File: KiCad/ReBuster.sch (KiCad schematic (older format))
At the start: 11 parts, among them U3 SN74CBTD16210, U4 SN74LVC16T245DGVR, U5 SN74CBTD16210, U6 SN74CBTD16210, U7 74LVC2T45DC, U8 PLCC_84_plug, U9 PLCC_84_plug

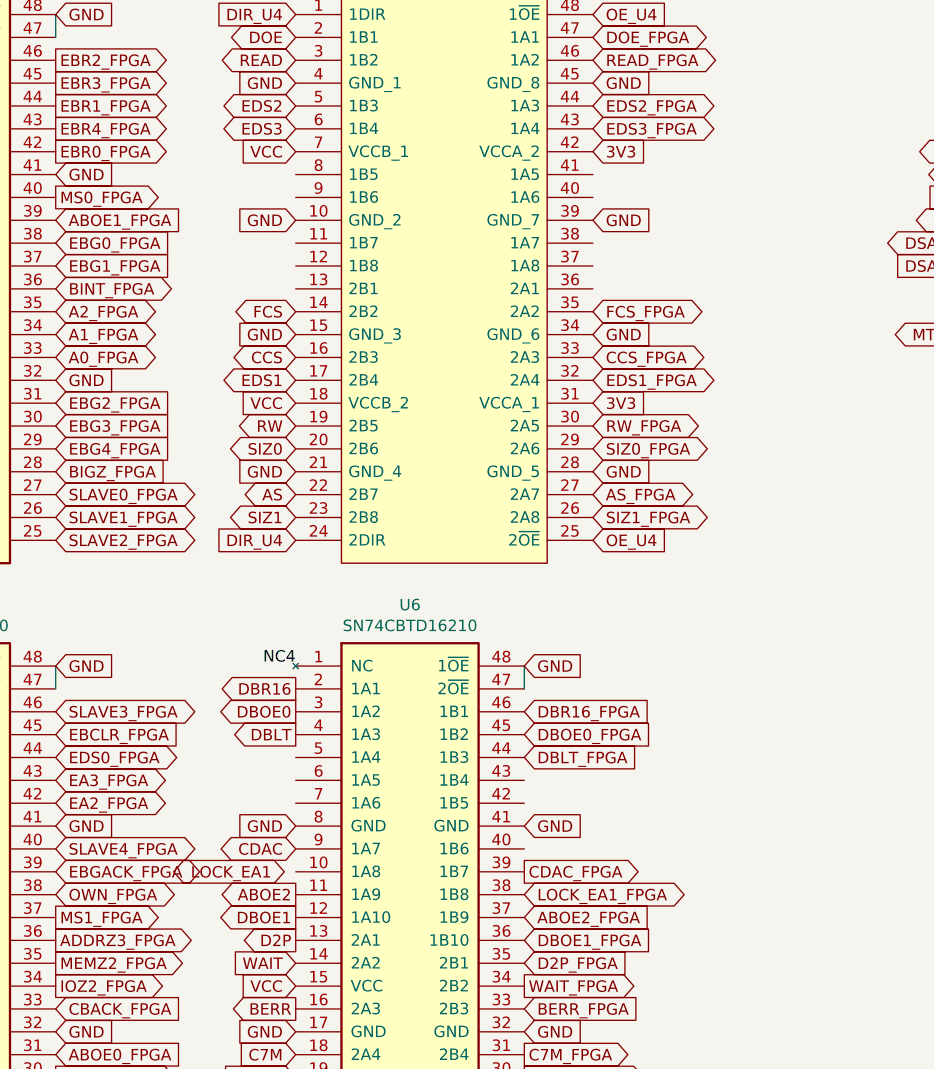
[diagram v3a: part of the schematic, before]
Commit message: Route EA1_LOCK to U4 (SN74LVC16T245DGVR) change K10 -> N4 in FPGA
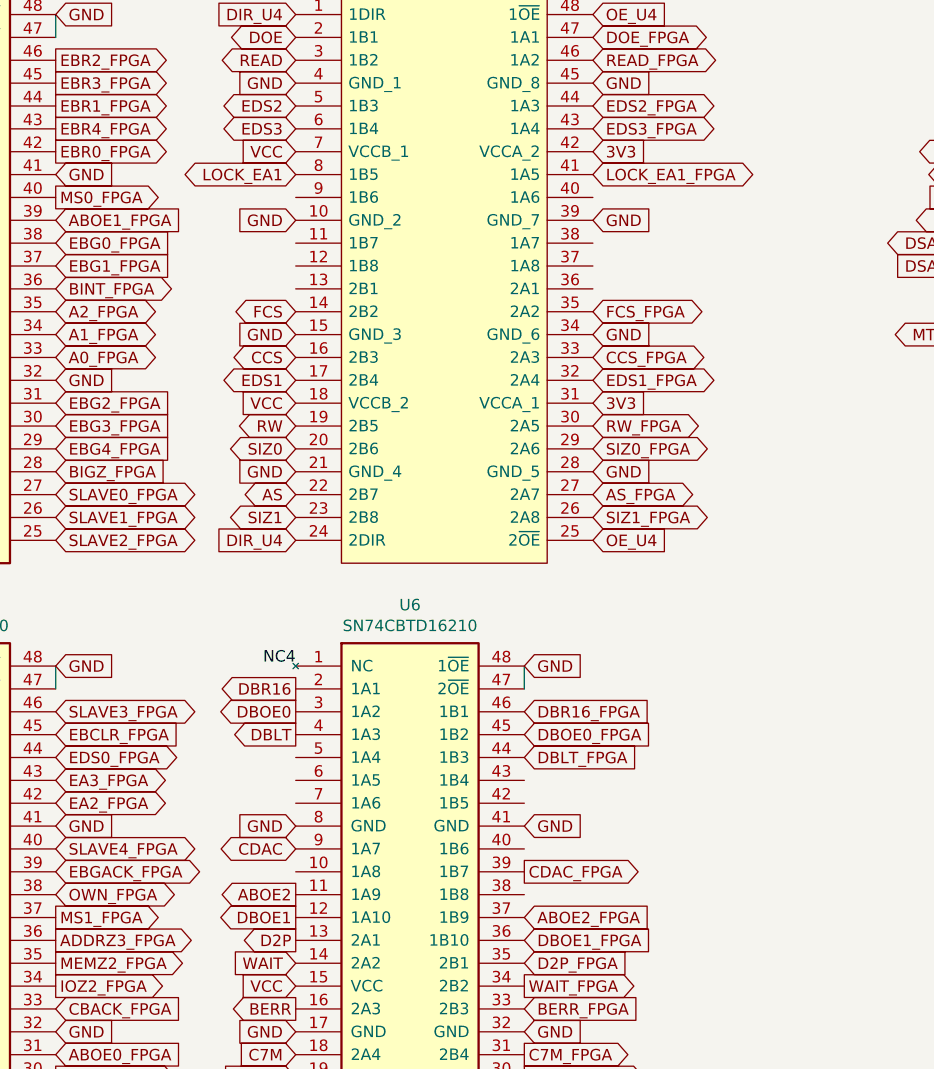
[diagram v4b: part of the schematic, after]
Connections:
- net LOCK_EA1: now also U4.8 (1B5)
- net LOCK_EA1_FPGA: now also U4.41 (1A5); no longer U6.38 (1B8)
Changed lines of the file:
@@
 Text GLabel 10200 4700 2    50   Output ~ 0
 CDAC_FPGA
-Text GLabel 10200 4800 2    50   BiDi ~ 0
+Text GLabel 10500 1650 2    50   BiDi ~ 0
 LOCK_EA1_FPGA
 Text GLabel 10200 4900 2    50   Input ~ 0
@@
 Text GLabel 9200 1450 0    50   BiDi ~ 0
 EDS3
-Text GLabel 9150 4700 0    50   BiDi ~ 0
+Text GLabel 9200 1650 0    50   BiDi ~ 0
 LOCK_EA1
 Text GLabel 9200 4800 0    50   Output ~ 0

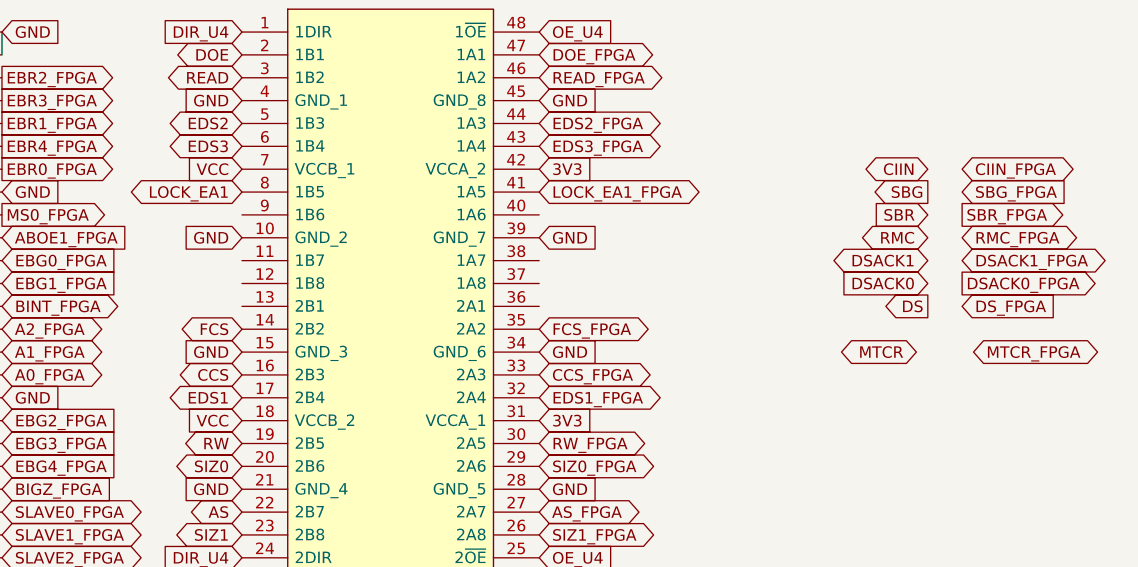
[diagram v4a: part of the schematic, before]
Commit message: Route MTCR to U4 (SN74LVC16T245DGVR) change F12 -> N5 in FPGA
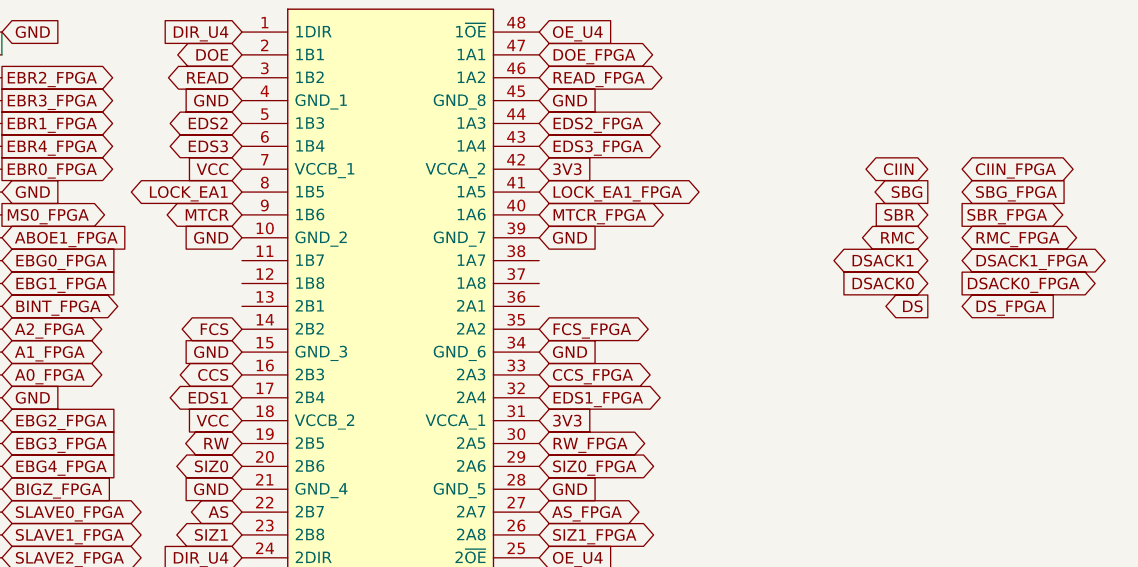
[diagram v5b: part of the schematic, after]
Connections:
- net MTCR: now also U4.9 (1B6)
- net MTCR_FPGA: now also U4.40 (1A6)
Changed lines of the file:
@@
 Text GLabel 8150 5700 2    50   Output ~ 0
 MS2_FPGA
-Text GLabel 12400 2350 2    50   BiDi ~ 0
+Text GLabel 10500 1750 2    50   BiDi ~ 0
 MTCR_FPGA
 Text GLabel 8150 5900 2    50   BiDi ~ 0
@@
 Text GLabel 7150 5700 0    50   Input ~ 0
 MS2
-Text GLabel 12150 2350 0    50   BiDi ~ 0
+Text GLabel 9200 1750 0    50   BiDi ~ 0
 MTCR
 Text GLabel 2750 4650 2    50   Output ~ 0

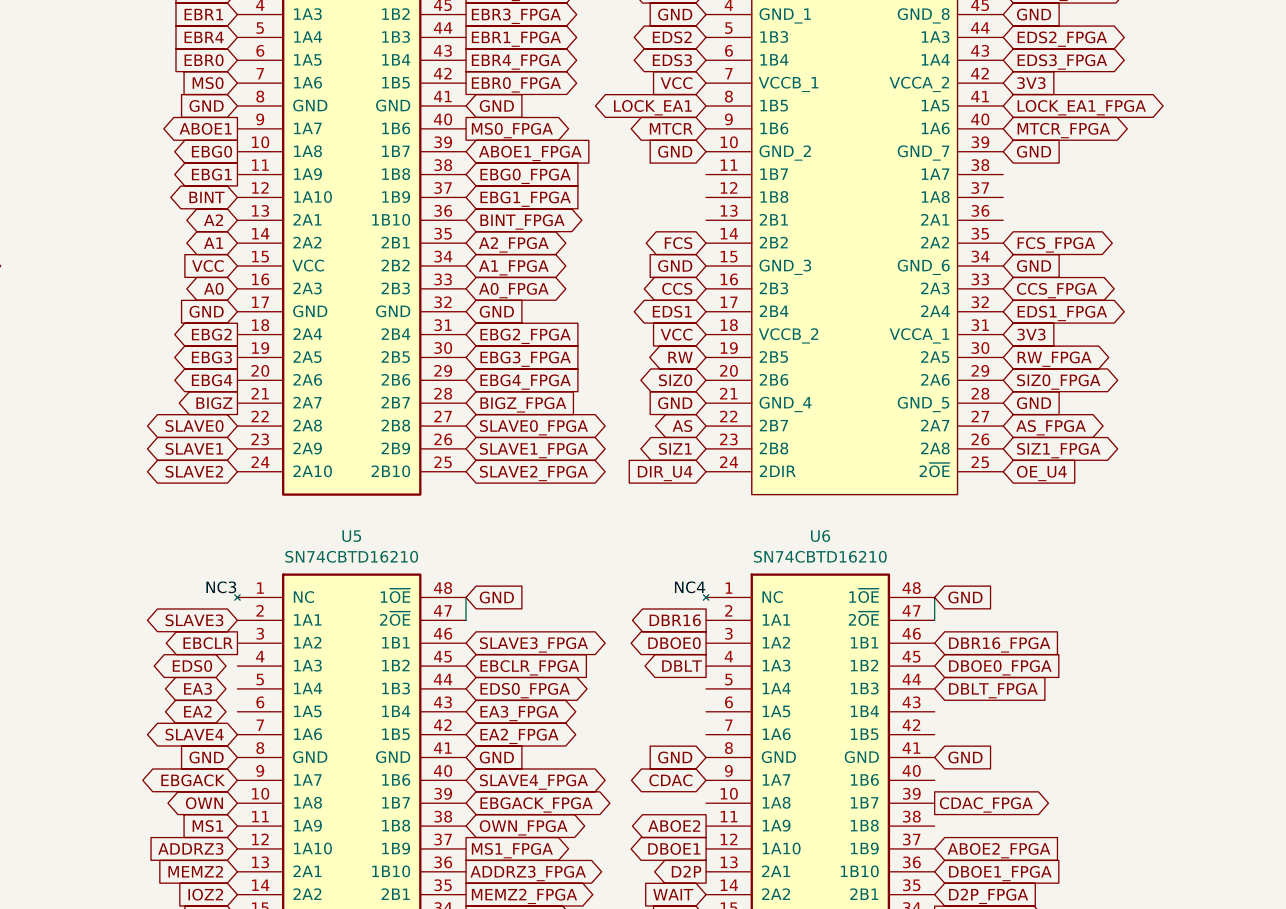
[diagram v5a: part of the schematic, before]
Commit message: Route EA2,EA3 to U4 (SN74LVC16T245DGVR) change D6 -> N6, B5 -> N7 in FPGA
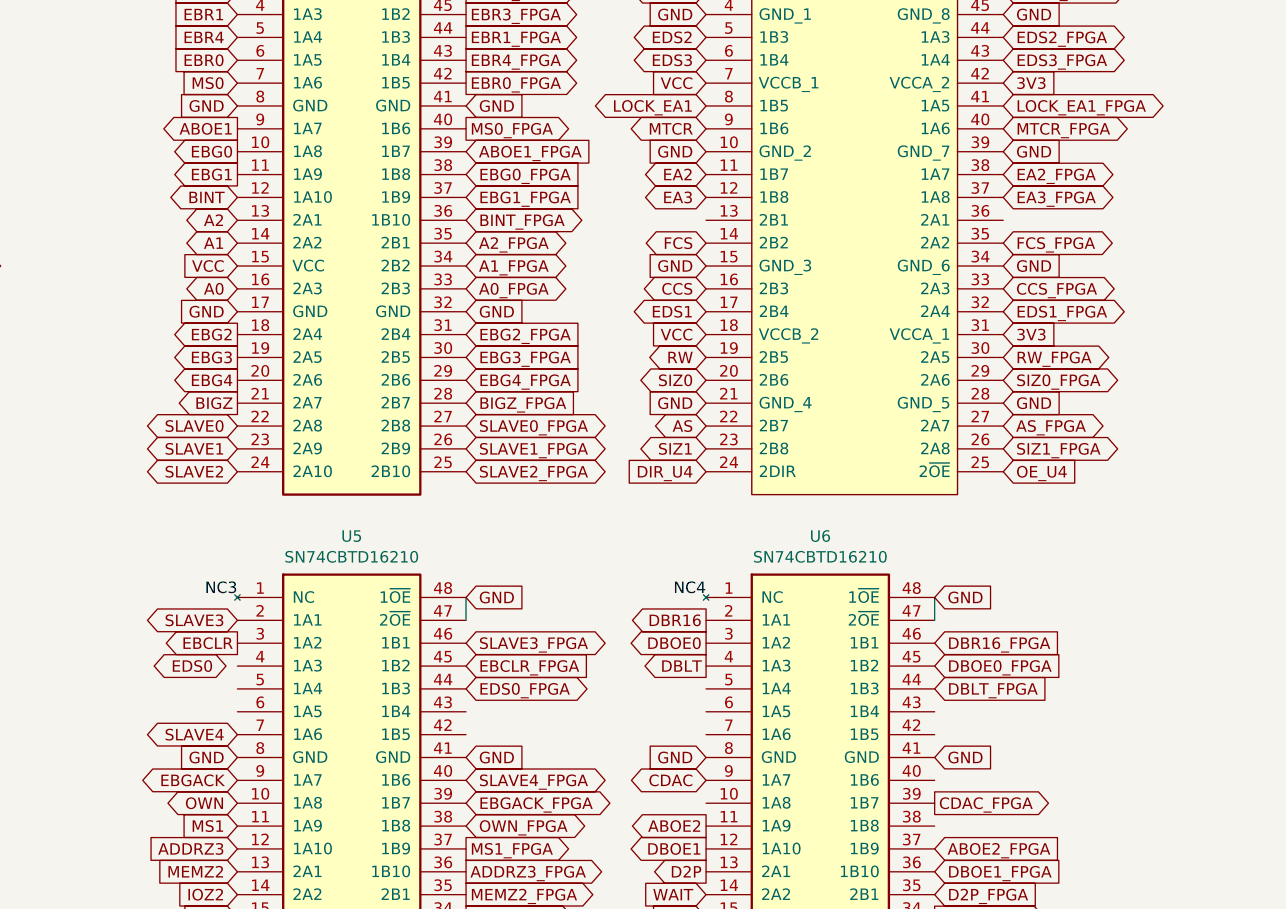
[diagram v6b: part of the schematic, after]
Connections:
- net EA2: now also U4.11 (1B7)
- net EA2_FPGA: now also U4.38 (1A7); no longer U5.42 (1B5)
- net EA3: now also U4.12 (1B8)
- net EA3_FPGA: now also U4.37 (1A8); no longer U5.43 (1B4)
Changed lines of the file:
@@
 Text GLabel 8150 4200 2    50   BiDi ~ 0
 EDS0_FPGA
-Text GLabel 8150 4300 2    50   BiDi ~ 0
+Text GLabel 10500 2050 2    50   BiDi ~ 0
 EA3_FPGA
-Text GLabel 8150 4400 2    50   BiDi ~ 0
+Text GLabel 10500 1950 2    50   BiDi ~ 0
 EA2_FPGA
 Text GLabel 8150 4700 2    50   BiDi ~ 0
@@
 Text GLabel 7150 4400 0    50   BiDi ~ 0
 SLAVE4
-Text GLabel 7100 4300 0    50   BiDi ~ 0
+Text GLabel 9200 1950 0    50   BiDi ~ 0
 EA2
-Text GLabel 7100 4200 0    50   BiDi ~ 0
+Text GLabel 9200 2050 0    50   BiDi ~ 0
 EA3
 Text GLabel 9200 2550 0    50   BiDi ~ 0

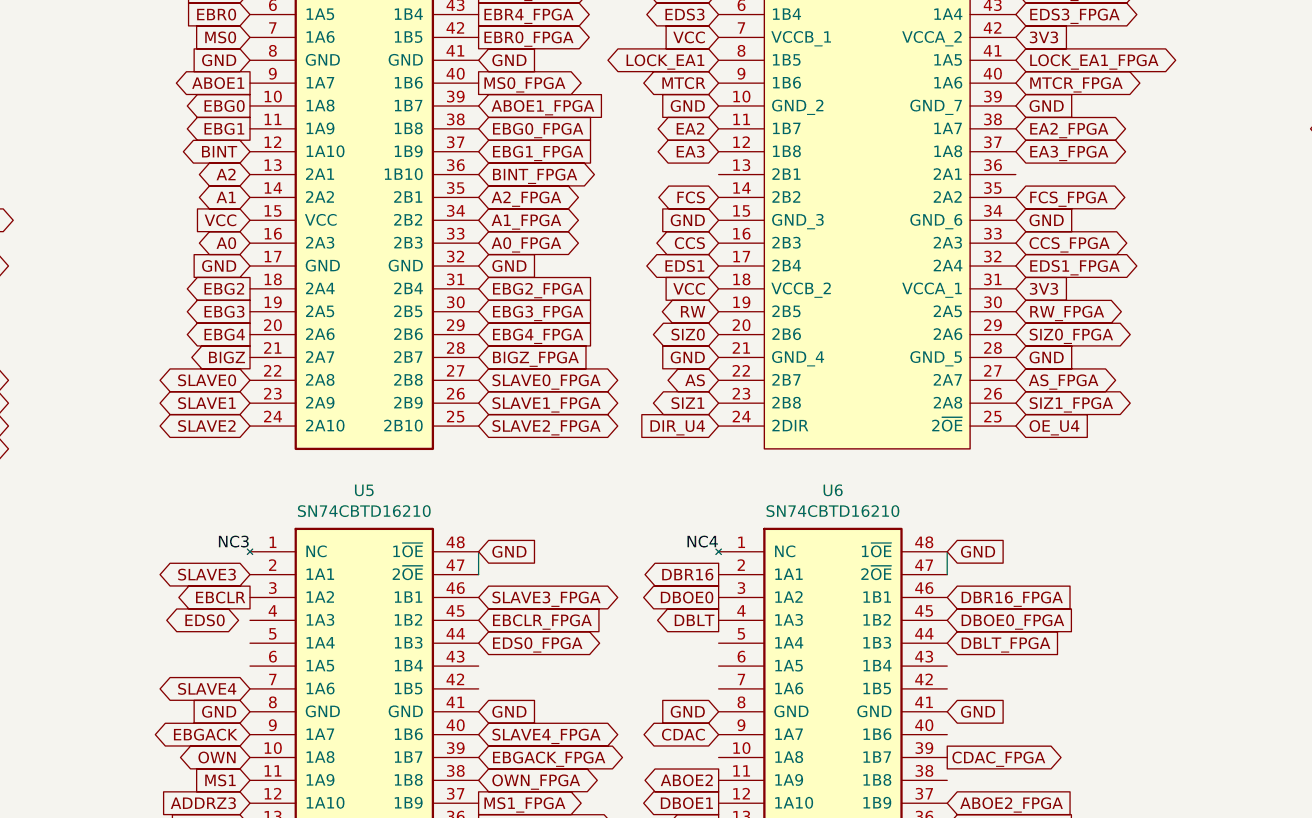
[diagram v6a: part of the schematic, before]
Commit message: Route EDS0 to U4 (SN74LVC16T245DGVR) change F4 -> N8 in FPGA
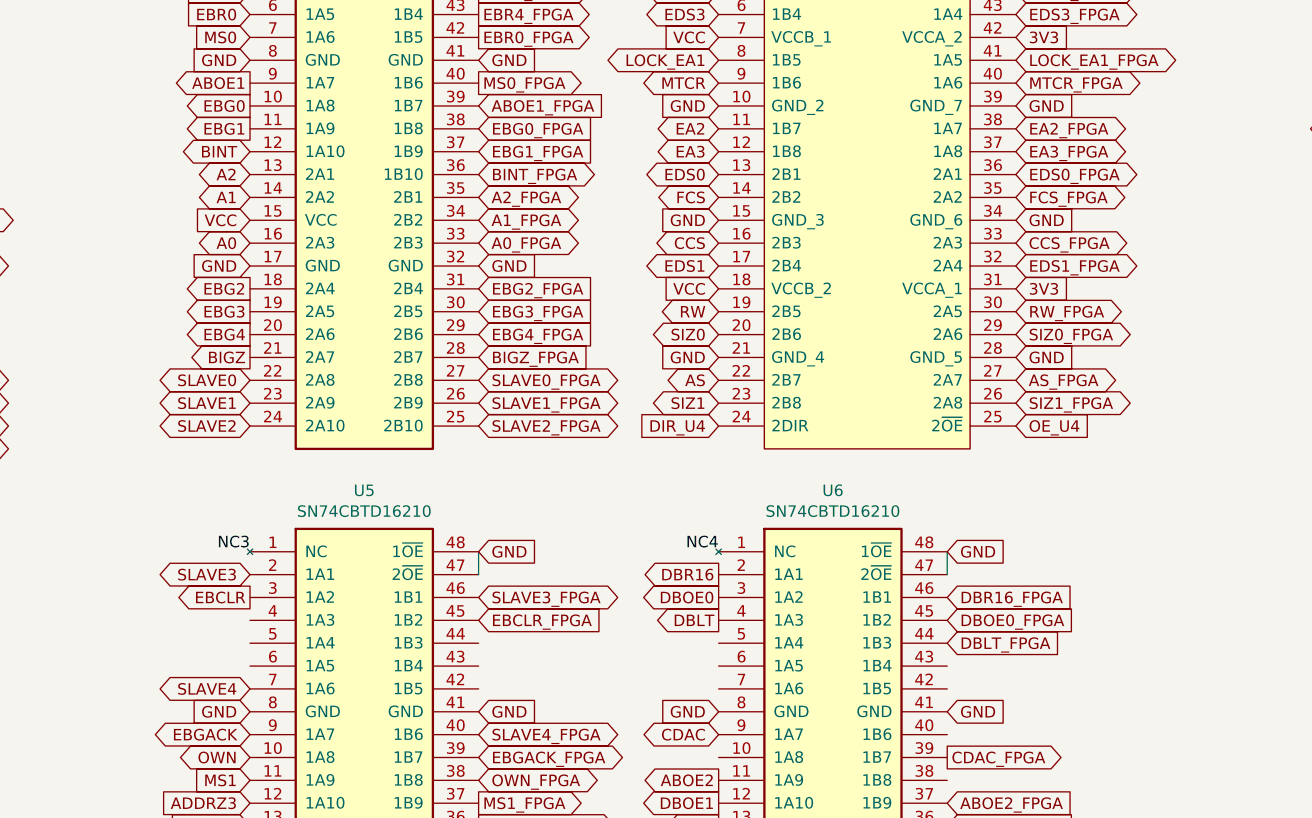
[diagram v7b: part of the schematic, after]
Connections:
- net EDS0: now also U4.13 (2B1)
- net EDS0_FPGA: now also U4.36 (2A1); no longer U5.44 (1B3)
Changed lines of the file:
@@
 Text GLabel 8150 4100 2    50   Input ~ 0
 EBCLR_FPGA
-Text GLabel 8150 4200 2    50   BiDi ~ 0
+Text GLabel 10500 2150 2    50   BiDi ~ 0
 EDS0_FPGA
 Text GLabel 10500 2050 2    50   BiDi ~ 0
@@
 Text GLabel 2750 2850 2    50   BiDi ~ 0
 EDS0
-Text GLabel 7100 4100 0    50   BiDi ~ 0
+Text GLabel 9200 2150 0    50   BiDi ~ 0
 EDS0
 $Comp
